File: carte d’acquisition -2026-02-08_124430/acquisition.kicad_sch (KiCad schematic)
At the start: 0 parts

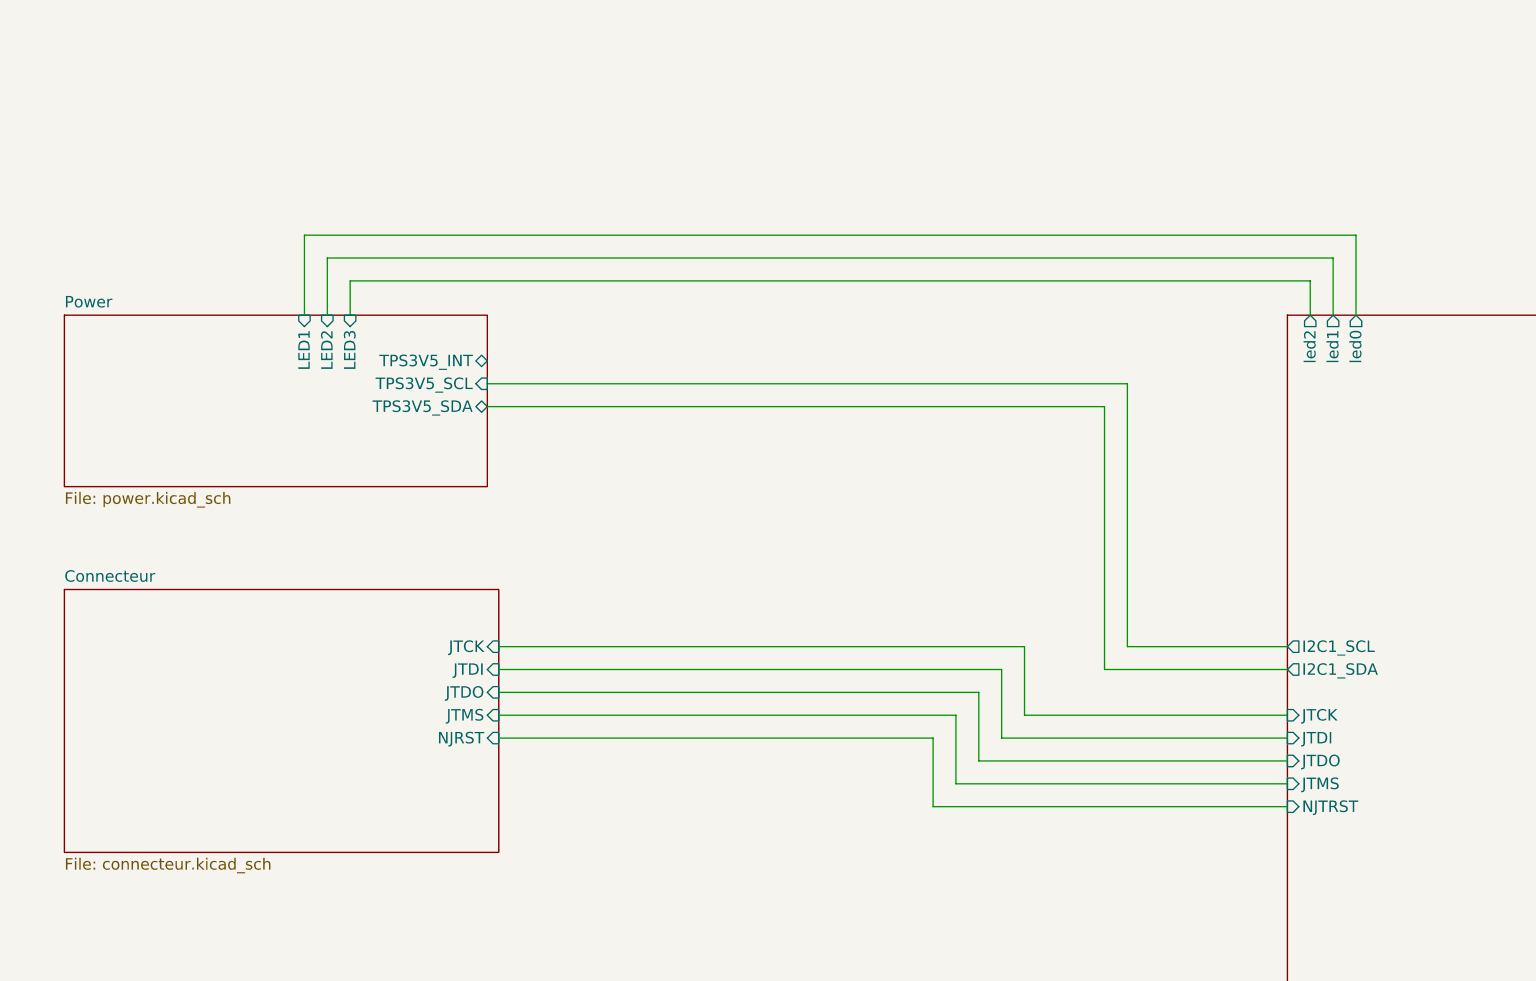
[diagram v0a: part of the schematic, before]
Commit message: Mis a jour plusieurs circuit et ajouter beaucoup de footprint manquant
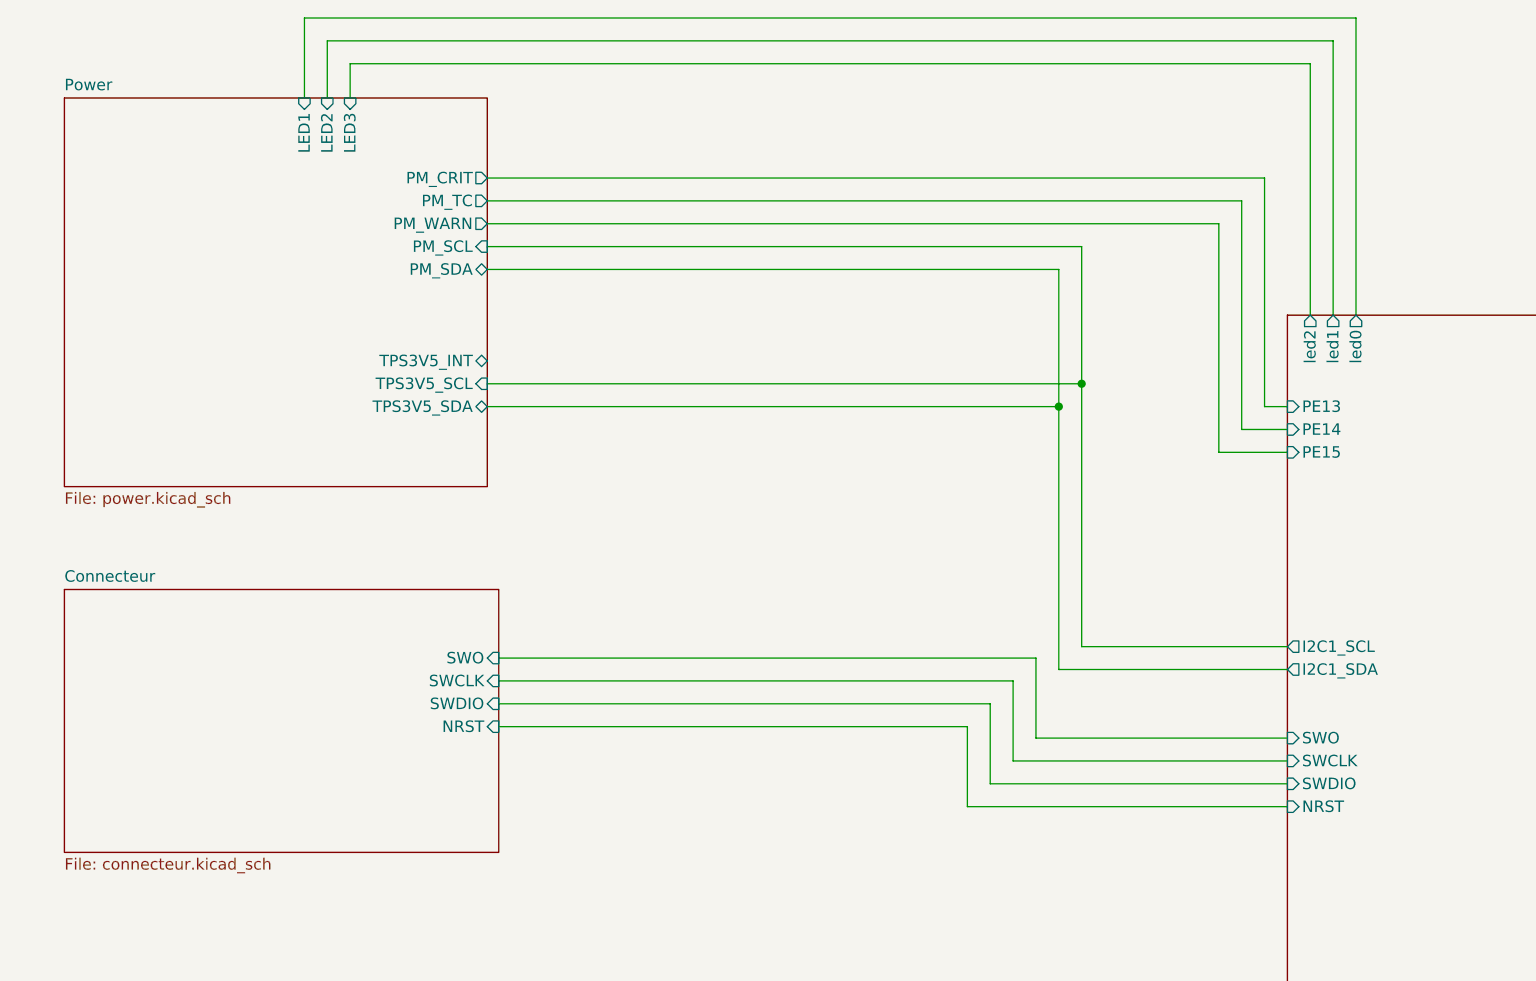
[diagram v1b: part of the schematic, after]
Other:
- sheet Connecteur ports: added NRST, SWCLK, SWDIO, SWO; removed JTCK, JTDI, JTDO, JTMS, NJRST
- sheet Microcontrolleur ports: added NRST, PE13, PE14, PE15, SWCLK, SWDIO, SWO; removed JTCK, JTDI, JTDO, JTMS, NJTRST
- sheet Power ports: added PM_CRIT, PM_SCL, PM_SDA, PM_TC, PM_WARN; removed none
